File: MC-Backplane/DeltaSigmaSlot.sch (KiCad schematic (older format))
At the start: 1 part, among them U3 86094328314755V1LF

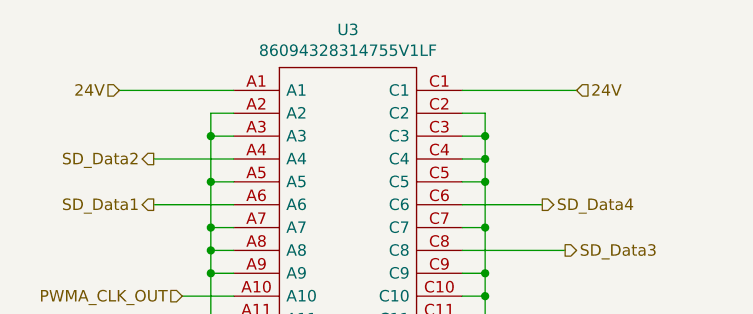
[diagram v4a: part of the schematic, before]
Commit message: added testpoints
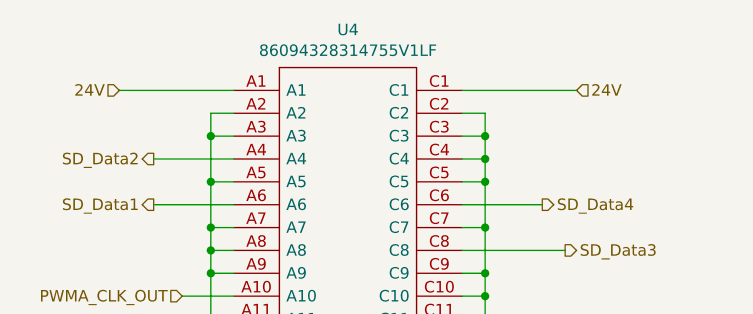
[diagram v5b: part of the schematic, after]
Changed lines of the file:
@@
 AR Path="/6231C7B7/622C3C12" Ref="U3"  Part="1"
 AR Path="/6234E41C/622C3C12" Ref="U4"  Part="1"
-F 0 "U3" H 5625 2740 50  0000 C CNN
+F 0 "U4" H 5625 2740 50  0000 C CNN
 F 1 "86094328314755V1LF" H 5625 2649 50  0000 C CNN
 F 2 "Footprints_MC-Backplane:86094328314755V1LF" V 5975 2575 50  0001 L CNN
